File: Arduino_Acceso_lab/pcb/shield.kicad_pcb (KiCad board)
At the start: 2 copper layers, 103.1 x 65.5 mm, 41 parts, among them K1 RELAY_C, K2 RELAY_C, P1 Power, P10 Sensor1, P11 Sensor2, P12 Luz1, P13 Luz2, P2 Analog, P3 Digital, P4 Digital, P5 modulo esp8266, P6 fuente, P7 buzzer 1, P8 buzzer 2, P9 Timer RTC, Q1 2N2222, Q2 2N2222, U1 LM2576

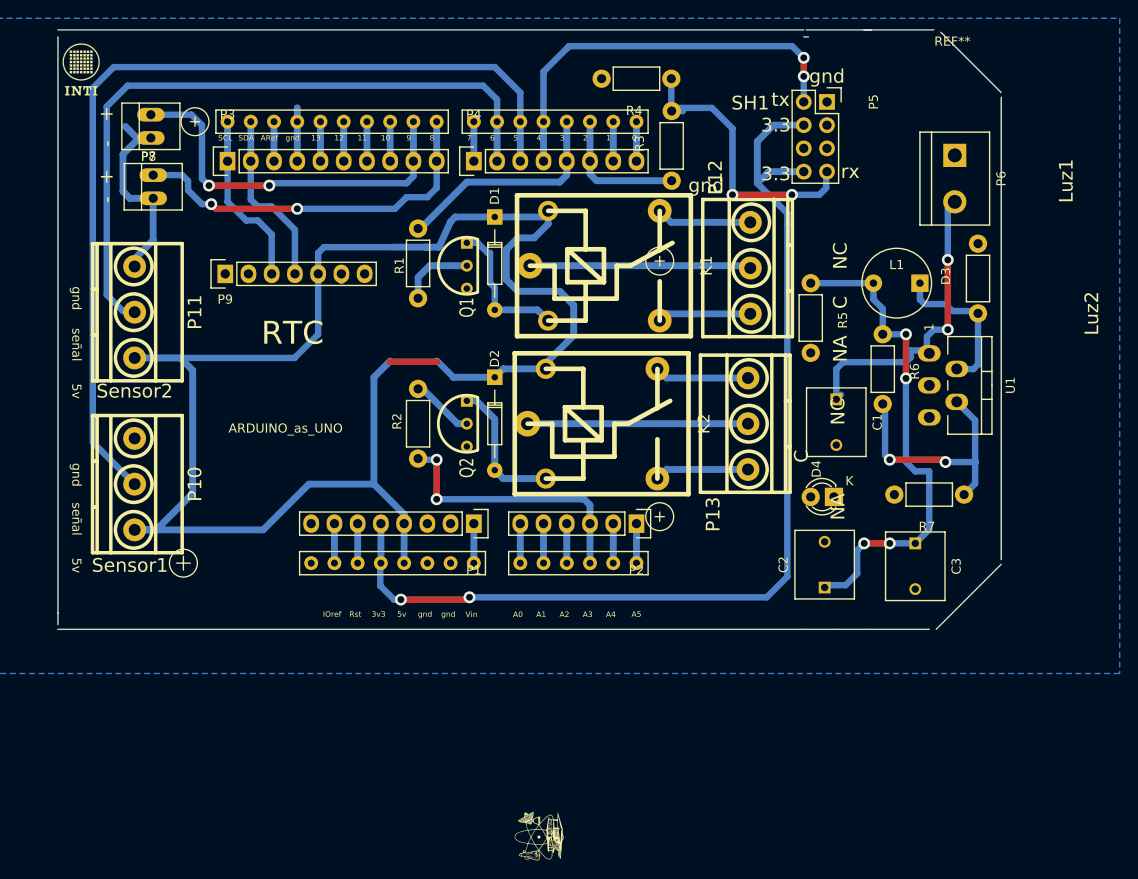
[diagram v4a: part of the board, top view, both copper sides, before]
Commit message: Detalles pcb acceso arduino lab.
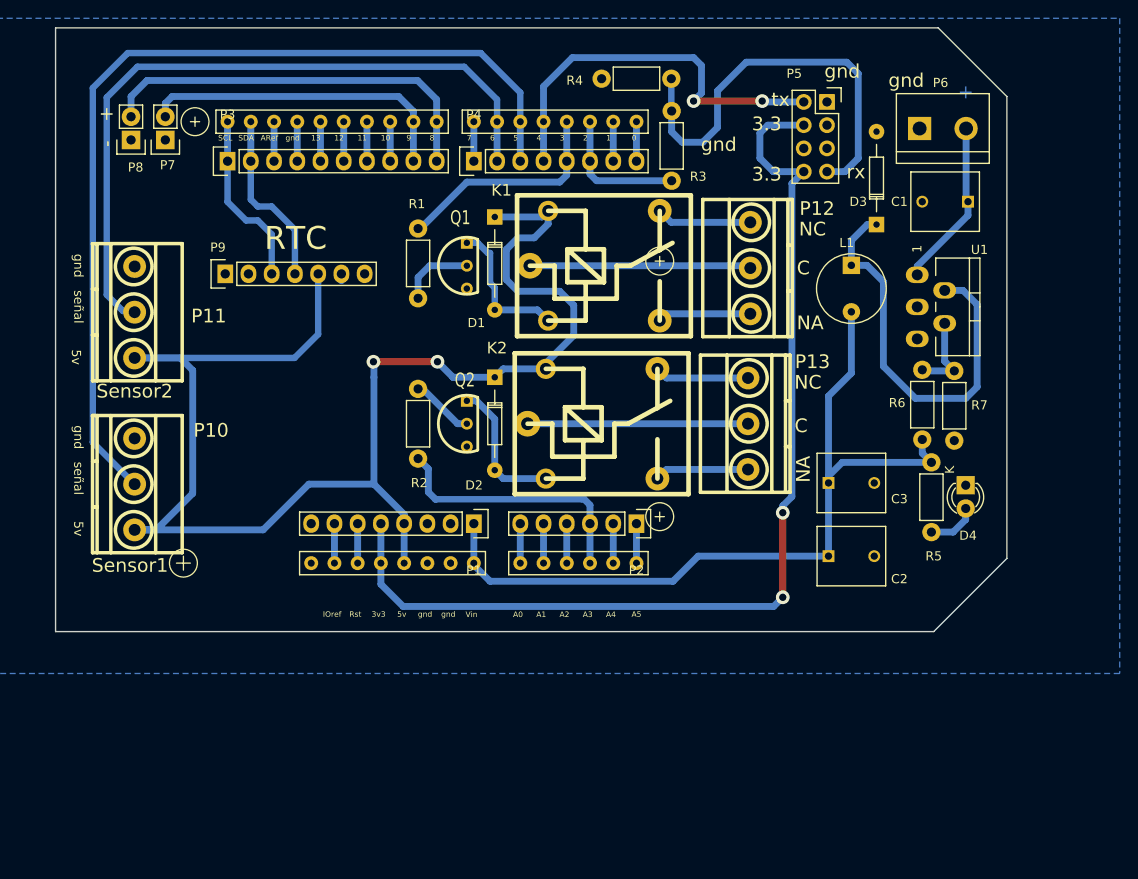
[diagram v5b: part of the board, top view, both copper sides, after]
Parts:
- removed ? (x4): , INTI
- removed G***: LOGO, Poncho_PLC:logoEscuela
- removed G***: LOGO, Poncho_PLC:logoInti
- removed REF**: INTI, INTI
- D3: footprint Resistors_ThroughHole:Resistor_Horizontal_RM7mm -> Diodes_ThroughHole:Diode_DO-35_SOD27_Horizontal_RM10
- P7, P8: footprint Connect:PINHEAD1-2 -> Pin_Headers:Pin_Header_Straight_1x02
- moved C1 26.0 mm to (211.2, 80.5), turned to 180 degrees
- moved R5 23.6 mm to (207.2, 109.0)
- moved D3 14.7 mm to (201.2, 83.0)
- moved D4 14.5 mm to (211.0, 111.5), turned to 270 degrees
- moved R7 13.6 mm to (209.8, 99.0), turned to 270 degrees
- moved R6 12.3 mm to (206.2, 106.5), turned to 90 degrees
- moved C3 11.6 mm to (196.0, 111.2), turned to 0 degrees
- moved U1 8.68 mm to (209.5, 92.0)
- moved P8 5.66 mm to (119.8, 73.8), turned to 180 degrees
- moved P6 5.63 mm to (208.5, 72.5), turned to 0 degrees
- moved L1 4.99 mm to (198.5, 90.0), turned to 270 degrees
- moved C2 3.46 mm to (196.0, 119.2), turned to 0 degrees
- moved P7 2.17 mm to (123.5, 73.8), turned to 180 degrees
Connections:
- net /3(**) renamed /REL1
- net /A3 renamed /REL2
- C2 pad 1: Net-(C2-Pad1) -> VDD
- C3 pad 1: Net-(C2-Pad1) -> VDD
- L1 pad 2: Net-(C2-Pad1) -> VDD
- P1 pad 1: Net-(P1-Pad1) -> VDD
- P1 pad 8: Net-(P1-Pad8) -> (no net)
- P4 pad 4: /rx-wifi -> /tx-wifi
- P4 pad 6: /tx-wifi -> /rx-wifi
- P5 pad 2: /rx-wifi -> /tx-wifi
- P5 pad 3: Net-(P5-Pad3) -> (no net)
- P5 pad 5: Net-(P5-Pad5) -> (no net)
- P5 pad 6: Net-(P5-Pad6) -> (no net)
- P9 pad 1: Net-(P9-Pad1) -> (no net)
- P9 pad 2: Net-(P9-Pad2) -> (no net)
- P9 pad 7: Net-(P9-Pad7) -> (no net)
- R3 pad 1: /tx-wifi -> /rx-wifi
- R5 pad 1: Net-(C2-Pad1) -> VDD
- R6 pad 1: Net-(C2-Pad1) -> VDD
- SH1 pad 2: /tx-wifi -> /rx-wifi
- SH1 pad 4: /rx-wifi -> /tx-wifi
- SH1 pad NC: Net-(SH1-PadNC) -> (no net)
- SH1 pad VIN: Net-(P1-Pad1) -> VDD
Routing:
- net VDD: track 0.00 -> 88.5 mm
- net Net-(C2-Pad1): track 54.6 -> 0.00 mm, vias 4 -> 0
- net /rx-wifi: track 44.8 -> 15.0 mm, vias 2 -> 0
- net /tx-wifi: track 15.0 -> 43.4 mm, vias 0 -> 2
- net Net-(D3-Pad1): track 16.9 -> 45.1 mm
- net GNDD: track 24.4 -> 1.68 mm
- net Net-(R6-Pad2): track 27.4 -> 9.18 mm, vias 2 -> 0
- net +5P: track 179.8 -> 161.7 mm, vias 0 -> 2
- net Net-(C1-Pad1): track 35.5 -> 18.4 mm, vias 2 -> 0
- net Net-(P5-Pad7): track 32.1 -> 47.2 mm, vias 2 -> 0
- net Net-(P3-Pad9): track 42.4 -> 35.4 mm, vias 2 -> 0
- net Net-(D4-Pad2): track 0.00 -> 5.53 mm
- net (no net): track 5.25 -> 0.00 mm
- net Net-(P1-Pad1): track 4.32 -> 0.00 mm
- net Net-(P3-Pad10): track 41.7 -> 44.3 mm, vias 2 -> 0
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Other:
- board size 103.1 x 65.5 mm -> 104 x 66 mm
